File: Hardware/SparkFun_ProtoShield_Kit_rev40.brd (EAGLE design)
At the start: 53.3 x 68.6 mm, 105 parts, among them SW2 MOMENTARY-SWITCH-SPST-PTH-6.0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

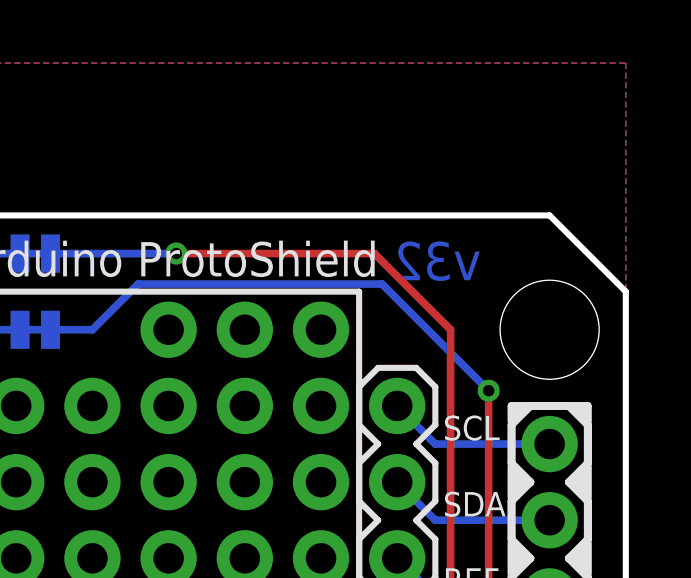
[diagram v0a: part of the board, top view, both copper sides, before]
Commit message: Update to v40
-Update SCH version number
-Update BRD version number in copper
-Update file names
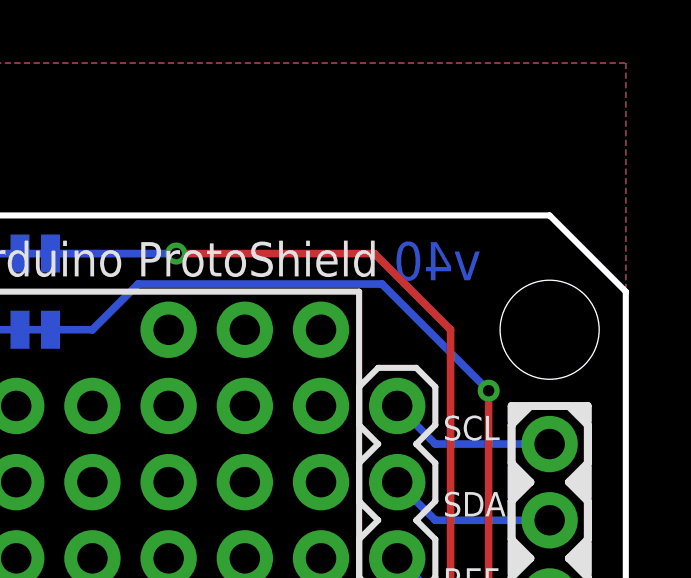
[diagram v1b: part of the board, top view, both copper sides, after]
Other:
- board text added: "v40"
- board text removed: "v32"
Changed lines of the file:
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@@
 <text x="4.826" y="2.667" size="0.8128" layer="21" font="vector" ratio="15">L1</text>
 <text x="17.2085" y="1.4605" size="0.8128" layer="21" font="vector" ratio="15" rot="R180">L2</text>
-<text x="45.593" y="62.611" size="1.27" layer="16" font="vector" ratio="15" rot="MR180">v32</text>
+<text x="45.593" y="62.611" size="1.27" layer="16" font="vector" ratio="15" rot="MR180">v40</text>
 <text x="30.099" y="3.1115" size="0.8128" layer="21" font="vector" ratio="15">5V</text>
 <text x="27.305" y="3.1115" size="0.8128" layer="21" font="vector" ratio="15">GND</text>
